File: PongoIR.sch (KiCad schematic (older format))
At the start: 31 parts, among them J1 Conn_01x04, J2 Conn_01x06, Q1 BC817, SW1 Reset, SW2 Learn, SW3 Shuffle, U1 TSOP348xx, U2 STM32F030C6Tx, Y1 16MHz

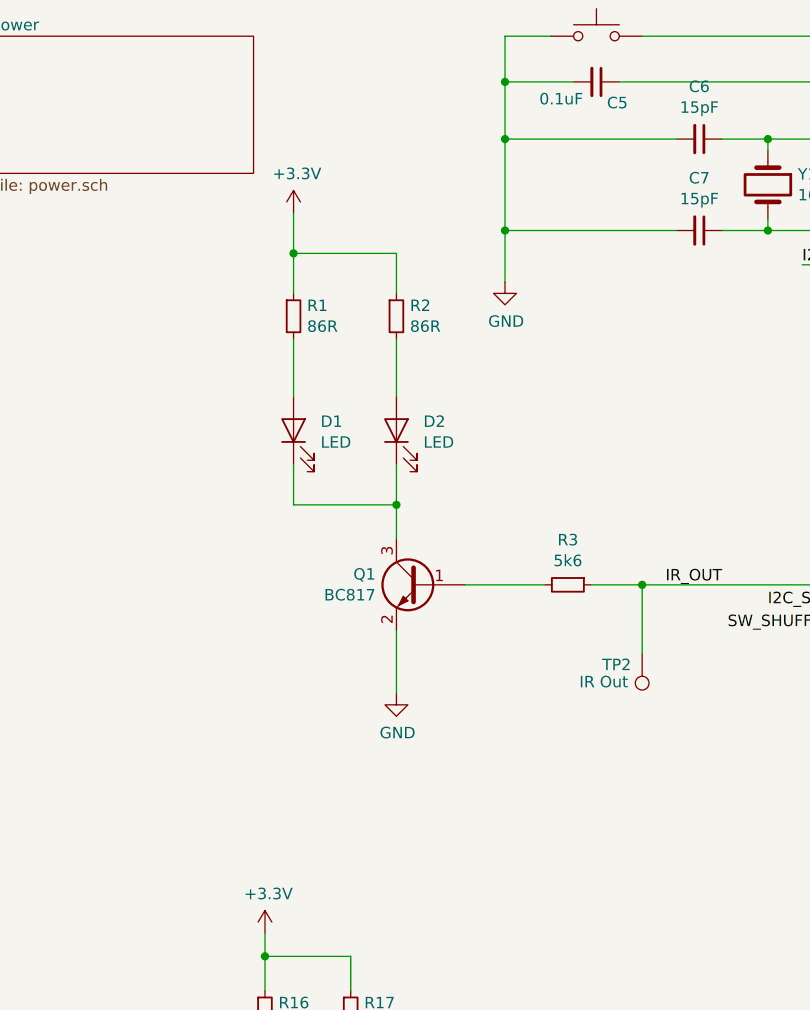
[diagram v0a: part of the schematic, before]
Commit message: change IR leds to NPN transistor
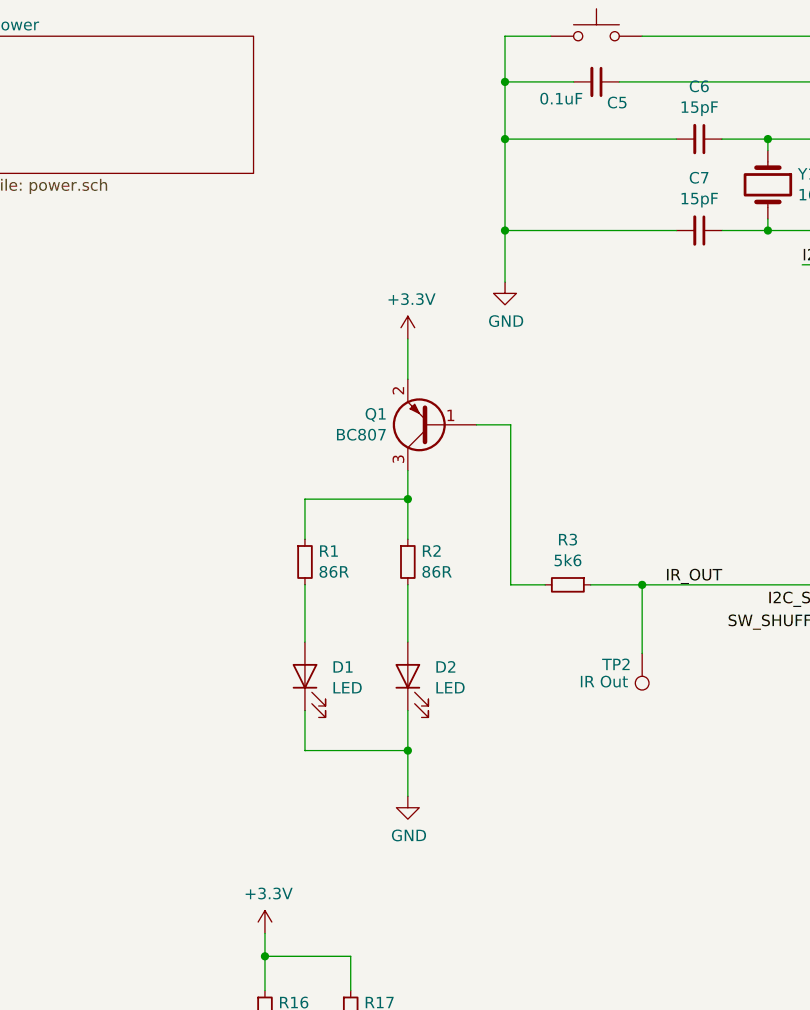
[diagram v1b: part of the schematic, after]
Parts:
- removed Q1: BC817, Package_TO_SOT_SMD:SOT-23, symbol Transistor_BJT:BC817
- added Q1: BC807, Package_TO_SOT_SMD:SOT-23, symbol Transistor_BJT:BC807
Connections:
- net +3V3: now also Q1.2 (E); no longer R1.1, R2.1
- net GND: now also D1.1 (K), D2.1 (K)
- net at R3.2: now also Q1.1 (B)
- new net: Q1.3 (C), R1.1, R2.1
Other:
- moved on the sheet: D1, D2, R1, R2
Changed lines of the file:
@@
 F4 "SDI" I L 7000 3800 50
 $EndSheet
-$Comp
-L Transistor_BJT:BC817 Q1
-U 1 1 62219ACD
-P 2625 4500
-F 0 "Q1" H 2816 4546 50  0000 L CNN
-F 1 "BC817" H 2816 4455 50  0000 L CNN
-F 2 "Package_TO_SOT_SMD:SOT-23" H 2825 4425 50  0001 L CIN
-F 3 "https://www.onsemi.com/pub/Collateral/BC818-D.pdf" H 2625 4500 50  0001 L CNN
-	1    2625 4500
-	-1   0    0    -1
-$EndComp
-Wire Wire Line
-	2525 4700 2525 4975
-$Comp
-L power:GND #PWR012
-U 1 1 6221D317
-P 2525 4975
-F 0 "#PWR012" H 2525 4725 50  0001 C CNN
-F 1 "GND" H 2530 4802 50  0000 C CNN
-F 2 "" H 2525 4975 50  0001 C CNN
-F 3 "" H 2525 4975 50  0001 C CNN
-	1    2525 4975
-	1    0    0    -1
-$EndComp
-$Comp
-L Device:LED D2
-U 1 1 6221EAEA
-P 2525 3825
-F 0 "D2" V 2564 3707 50  0000 R CNN
-F 1 "LED" V 2473 3707 50  0000 R CNN
-F 2 "LED_THT:LED_D5.0mm_Horizontal_O1.27mm_Z3.0mm_IRGrey" H 2525 3825 50  0001 C CNN
-F 3 "~" H 2525 3825 50  0001 C CNN
-	1    2525 3825
-	0    -1   -1   0
-$EndComp
-Wire Wire Line
-	2075 3975 2075 4150
-Wire Wire Line
-	2075 4150 2525 4150
-Wire Wire Line
-	2525 4150 2525 4300
-Wire Wire Line
-	2525 3975 2525 4150
-Connection ~ 2525 4150
-$Comp
-L Device:R_Small R2
-U 1 1 62220D32
-P 2525 3325
-F 0 "R2" H 2584 3371 50  0000 L CNN
-F 1 "86R" H 2584 3280 50  0000 L CNN
-F 2 "Resistor_SMD:R_0402_1005Metric" H 2525 3325 50  0001 C CNN
-F 3 "~" H 2525 3325 50  0001 C CNN
-	1    2525 3325
-	1    0    0    -1
-$EndComp
-Wire Wire Line
-	2525 3425 2525 3675
-Wire Wire Line
-	2075 3425 2075 3675
-Wire Wire Line
-	2075 3225 2075 3050
-Wire Wire Line
-	2075 3050 2525 3050
-Wire Wire Line
-	2525 3050 2525 3225
-Connection ~ 2075 3050
-Wire Wire Line
-	2075 3050 2075 2875
+Wire Wire Line
+	2575 4500 2575 4750
+Wire Wire Line
+	2575 3600 2575 3425
 $Comp
 L power:+3.3V #PWR08
 U 1 1 62223F58
-P 2075 2875
-F 0 "#PWR08" H 2075 2725 50  0001 C CNN
-F 1 "+3.3V" H 2090 3048 50  0000 C CNN
-F 2 "" H 2075 2875 50  0001 C CNN
-F 3 "" H 2075 2875 50  0001 C CNN
-	1    2075 2875
+P 2575 3425
+F 0 "#PWR08" H 2575 3275 50  0001 C CNN
+F 1 "+3.3V" H 2590 3598 50  0000 C CNN
+F 2 "" H 2575 3425 50  0001 C CNN
+F 3 "" H 2575 3425 50  0001 C CNN
+	1    2575 3425
 	1    0    0    -1
 $EndComp
@@
 Wire Wire Line
 	4425 2300 4775 2300
-$Comp
-L Device:R_Small R1
-U 1 1 621FA3C9
-P 2075 3325
-F 0 "R1" H 2134 3371 50  0000 L CNN
-F 1 "86R" H 2134 3280 50  0000 L CNN
-F 2 "Resistor_SMD:R_0402_1005Metric" H 2075 3325 50  0001 C CNN
-F 3 "~" H 2075 3325 50  0001 C CNN
-	1    2075 3325
-	1    0    0    -1
-$EndComp
 $Comp
 L Switch:SW_Push SW1
@@
 Wire Wire Line
 	4675 2500 4775 2500
-Wire Wire Line
-	2825 4500 3175 4500
 Wire Wire Line
 	8325 3700 8325 4200
@@
 NoConn ~ 5975 5100
 $Comp
-L Device:LED D1
-U 1 1 62254DED
-P 2075 3825
-F 0 "D1" V 2114 3707 50  0000 R CNN
-F 1 "LED" V 2023 3707 50  0000 R CNN
-F 2 "LED_THT:LED_D5.0mm_Horizontal_O1.27mm_Z3.0mm_IRGrey" H 2075 3825 50  0001 C CNN
-F 3 "~" H 2075 3825 50  0001 C CNN
-	1    2075 3825
-	0    -1   -1   0
-$EndComp
-$Comp
 L Switch:SW_Push SW3
 U 1 1 622B5B53
@@
 Wire Wire Line
 	1950 6625 2575 6625
+Wire Wire Line
+	3025 4500 3175 4500
+$Comp
+L Transistor_BJT:BC807 Q1
+U 1 1 627042F1
+P 2675 3800
+F 0 "Q1" H 2866 3754 50  0000 L CNN
+F 1 "BC807" H 2866 3845 50  0000 L CNN
+F 2 "Package_TO_SOT_SMD:SOT-23" H 2875 3725 50  0001 L CIN
+F 3 "http://www.fairchildsemi.com/ds/BC/BC807.pdf" H 2675 3800 50  0001 L CNN
+	1    2675 3800
+	-1   0    0    1
+$EndComp
+Wire Wire Line
+	2875 3800 3025 3800
+Wire Wire Line
+	3025 3800 3025 4500
+Wire Wire Line
+	2575 5225 2575 5425
+Connection ~ 2575 5225
+Wire Wire Line
+	2575 5050 2575 5225
+Wire Wire Line
+	2575 4125 2575 4300
+$Comp
+L Device:LED D1
+U 1 1 62254DED
+P 2125 4900
+F 0 "D1" V 2164 4782 50  0000 R CNN
+F 1 "LED" V 2073 4782 50  0000 R CNN
+F 2 "LED_THT:LED_D5.0mm_Horizontal_O1.27mm_Z3.0mm_IRGrey" H 2125 4900 50  0001 C CNN
+F 3 "~" H 2125 4900 50  0001 C CNN
+	1    2125 4900
+	0    -1   -1   0
+$EndComp
+$Comp
+L Device:R_Small R1
+U 1 1 621FA3C9
+P 2125 4400
+F 0 "R1" H 2184 4446 50  0000 L CNN
+F 1 "86R" H 2184 4355 50  0000 L CNN
+F 2 "Resistor_SMD:R_0402_1005Metric" H 2125 4400 50  0001 C CNN
+F 3 "~" H 2125 4400 50  0001 C CNN
+	1    2125 4400
+	1    0    0    -1
+$EndComp
+Wire Wire Line
+	2125 4125 2575 4125
+Wire Wire Line
+	2125 4300 2125 4125
+Wire Wire Line
+	2125 4500 2125 4750
+$Comp
+L Device:R_Small R2
+U 1 1 62220D32
+P 2575 4400
+F 0 "R2" H 2634 4446 50  0000 L CNN
+F 1 "86R" H 2634 4355 50  0000 L CNN
+F 2 "Resistor_SMD:R_0402_1005Metric" H 2575 4400 50  0001 C CNN
+F 3 "~" H 2575 4400 50  0001 C CNN
+	1    2575 4400
+	1    0    0    -1
+$EndComp
+Wire Wire Line
+	2125 5225 2575 5225
+Wire Wire Line
+	2125 5050 2125 5225
+$Comp
+L Device:LED D2
+U 1 1 6221EAEA
+P 2575 4900
+F 0 "D2" V 2614 4782 50  0000 R CNN
+F 1 "LED" V 2523 4782 50  0000 R CNN
+F 2 "LED_THT:LED_D5.0mm_Horizontal_O1.27mm_Z3.0mm_IRGrey" H 2575 4900 50  0001 C CNN
+F 3 "~" H 2575 4900 50  0001 C CNN
+	1    2575 4900
+	0    -1   -1   0
+$EndComp
+$Comp
+L power:GND #PWR012
+U 1 1 6221D317
+P 2575 5425
+F 0 "#PWR012" H 2575 5175 50  0001 C CNN
+F 1 "GND" H 2580 5252 50  0000 C CNN
+F 2 "" H 2575 5425 50  0001 C CNN
+F 3 "" H 2575 5425 50  0001 C CNN
+	1    2575 5425
+	1    0    0    -1
+$EndComp
+Wire Wire Line
+	2575 4000 2575 4125
+Connection ~ 2575 4125
 $EndSCHEMATC
